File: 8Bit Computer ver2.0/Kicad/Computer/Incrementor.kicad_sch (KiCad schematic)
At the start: 5 parts, among them IC50 SN74LVC1G14DBVR, IC51 SN74LVC1G32DBVR, IC52 SN74HCS74DR, IC53 SN74HCS86DR, IC54 SN74HCS86DR

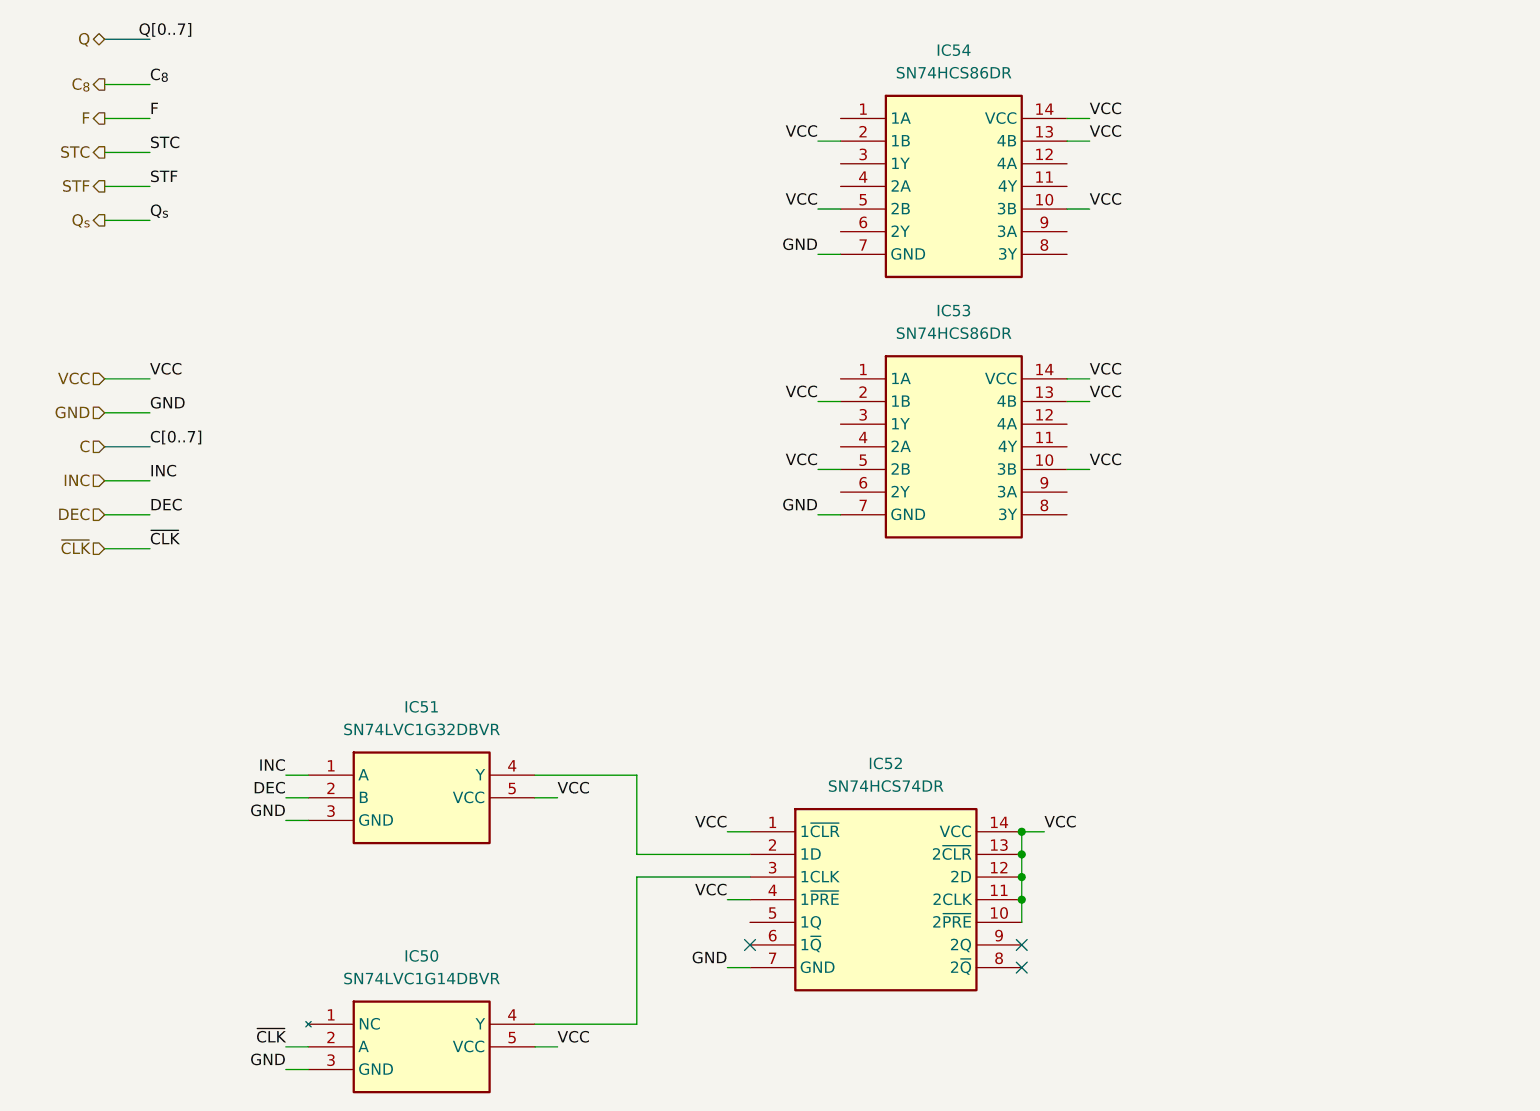
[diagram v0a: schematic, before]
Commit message: parts,Kicad
parts:
changed 8xDlatch HCS to ABT 574
waiting for SRAM CAD Model
Kicad:
imported AHC types of ICs
added ProgrammeCounter
finished Comparator
changed all HCS to AHC except 3in OR ->no AHC Version
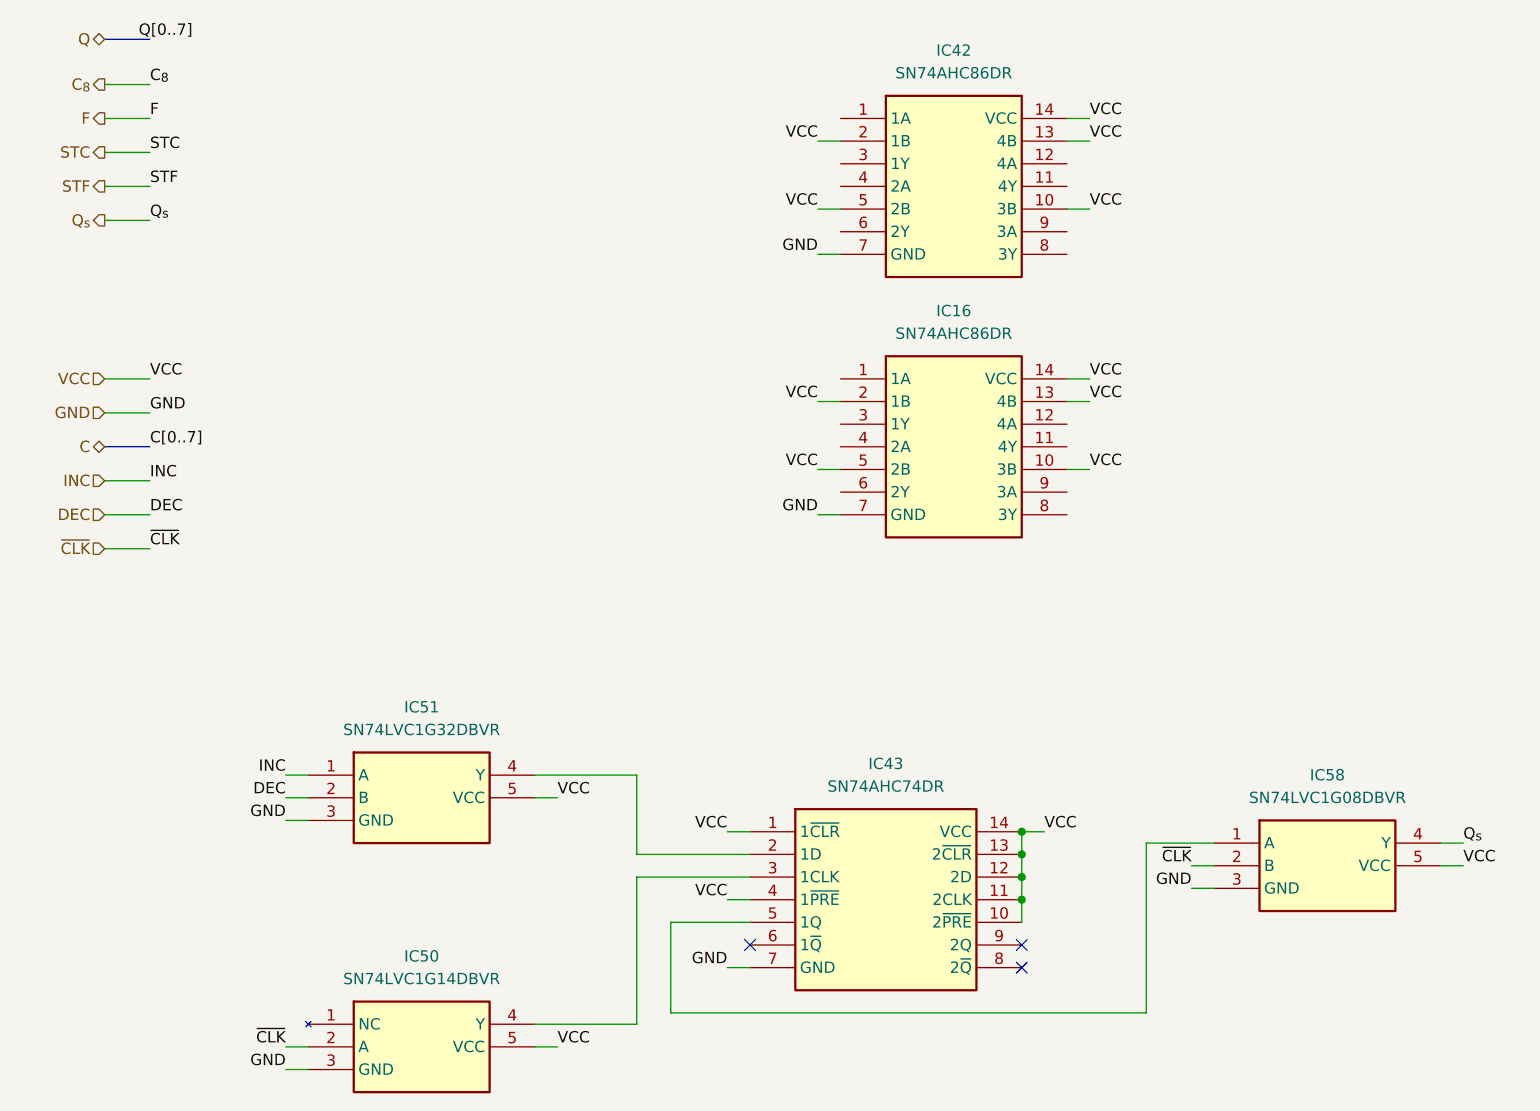
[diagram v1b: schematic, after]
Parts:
- removed IC52: SN74HCS74DR, Samacsys:SOIC127P600X175-14N, symbol Samacsys:SN74HCS74DR
- removed IC53, IC54: SN74HCS86DR, Samacsys:SOIC127P600X175-14N, symbol Samacsys:SN74HCS86DR
- added IC16, IC42: SN74AHC86DR, Samacsys:SOIC127P600X175-14N, symbol Samacsys:SN74AHC86DR
- added IC43: SN74AHC74DR, Samacsys:SOIC127P600X175-14N, symbol Samacsys:SN74AHC74DR
- added IC58: SN74LVC1G08DBVR, Samacsys:SOT95P280X145-5N, symbol Samacsys:SN74LVC1G08DBVR
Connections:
- net GND: now also IC16.7 (GND), IC42.7 (GND), IC43.7 (GND), IC58.3 (GND)
- net Q_{s}: now also IC58.4 (Y)
- net VCC: now also IC16.10 (3B), IC16.13 (4B), IC16.14 (VCC), IC16.2 (1B), IC16.5 (2B), IC42.10 (3B), IC42.13 (4B), IC42.14 (VCC), IC42.2 (1B), IC42.5 (2B), IC43.1 (1~{CLR}), IC43.10 (2~{PRE}), IC43.11 (2CLK), IC43.12 (2D), IC43.13 (2~{CLR}), IC43.14 (VCC), IC43.4 (1~{PRE}), IC58.5 (VCC)
- net ~{CLK}: now also IC58.2 (B)
- net at IC51.4 (Y): now also IC43.2 (1D)
- net at IC50.4 (Y): now also IC43.3 (1CLK)
- new net: IC43.5 (1Q), IC58.1 (A)

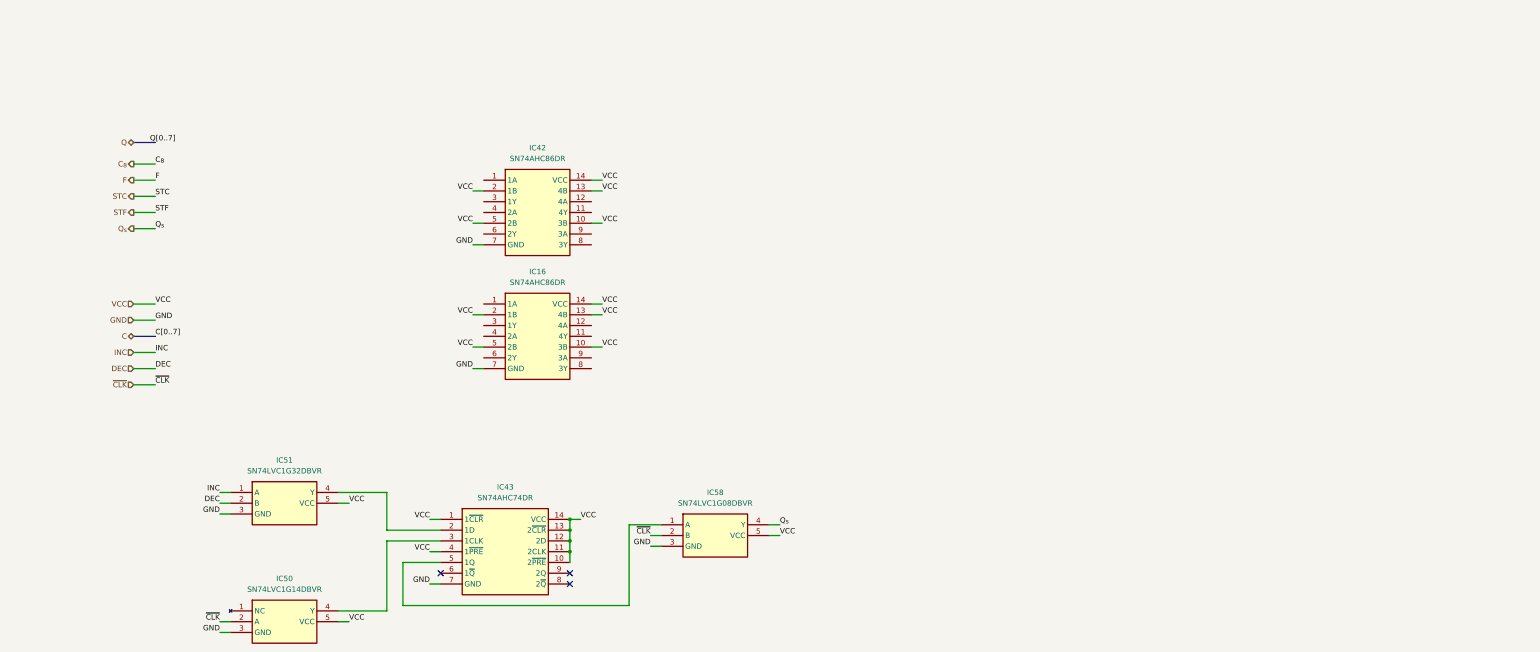
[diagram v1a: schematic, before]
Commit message: partsList, Kicad
parts:
added faster Comparator 521
added 1CH XOR
added 8Bit and 16Bit Driver 245, 16245
->they need pullUp resistors for High-Z when power on
Kicad:
included SRAM CAD Model AS7C1024
included some CAD Models
added Register 1 0x20 and 0x21
finished Incrementor
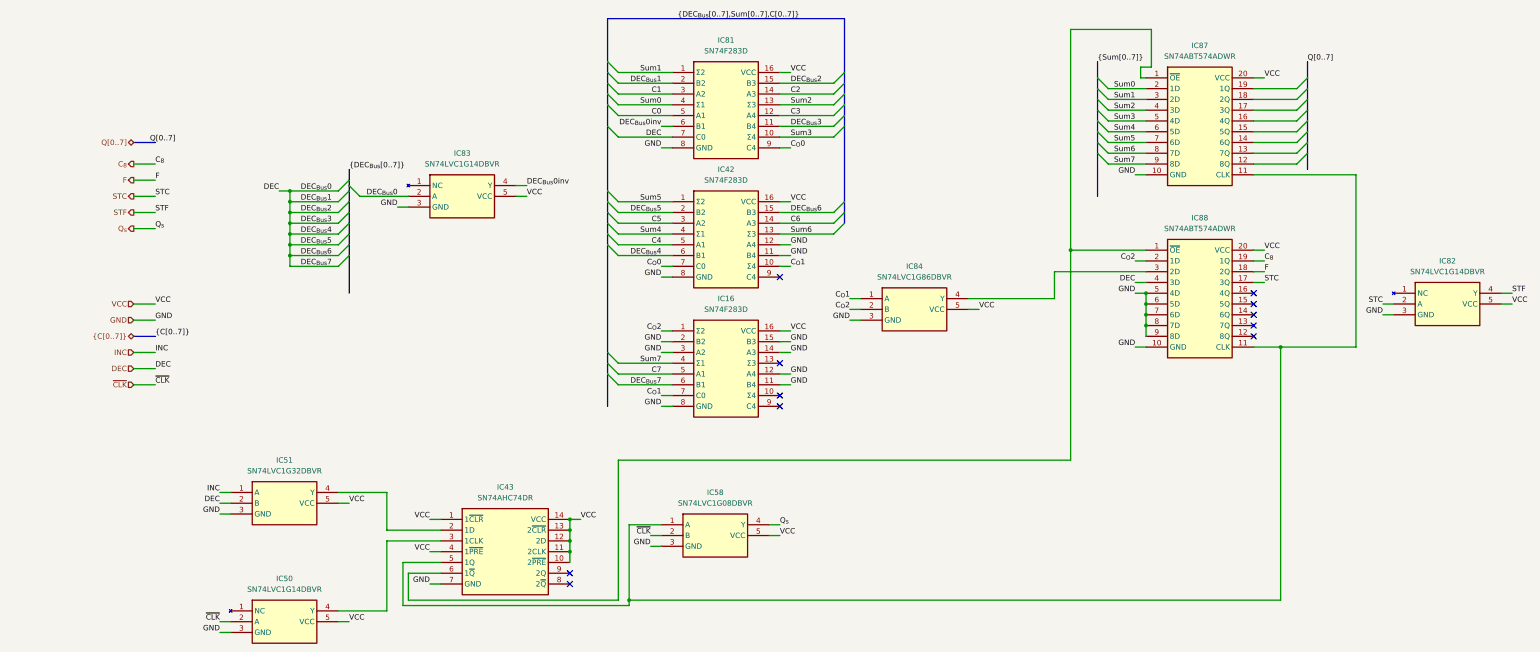
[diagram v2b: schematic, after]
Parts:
- removed IC16, IC42: SN74AHC86DR, Samacsys:SOIC127P600X175-14N, symbol Samacsys:SN74AHC86DR
- added IC16, IC42, IC81: SN74F283D, Samacsys:SOIC127P600X175-16N, symbol Samacsys:SN74F283D
- added IC82, IC83: SN74LVC1G14DBVR, Samacsys:SOT95P280X145-5N, symbol Samacsys:SN74LVC1G14DBVR
- added IC84: SN74LVC1G86DBVR, Samacsys:SOT95P280X145-5N, symbol Samacsys:SN74LVC1G86DBVR
- added IC87, IC88: SN74ABT574ADWR, Samacsys:SOIC127P1030X265-20N, symbol Samacsys:SN74ABT574ADWR
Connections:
- net C_{8}: now also IC88.19 (1Q)
- net DEC: now also IC16.6 (B1), IC42.15 (B3), IC42.2 (B2), IC42.6 (B1), IC81.11 (B4), IC81.15 (B3), IC81.2 (B2), IC81.7 (C0), IC83.2 (A), IC88.4 (3D)
- net F: now also IC88.18 (2Q)
- net GND: now also IC16.11 (B4), IC16.12 (A4), IC16.14 (A3), IC16.15 (B3), IC16.2 (B2), IC16.3 (A2), IC16.8 (GND), IC42.11 (B4), IC42.12 (A4), IC42.8 (GND), IC81.8 (GND), IC82.3 (GND), IC83.3 (GND), IC84.3 (GND), IC87.10 (GND), IC88.10 (GND), IC88.5 (4D), IC88.6 (5D), IC88.7 (6D), IC88.8 (7D), IC88.9 (8D)
- net STC: now also IC82.2 (A), IC88.17 (3Q)
- net STF: now also IC82.4 (Y)
- net VCC: now also IC16.16 (VCC), IC42.16 (VCC), IC81.16 (VCC), IC82.5 (VCC), IC83.5 (VCC), IC84.5 (VCC), IC87.20 (VCC), IC88.20 (VCC)
- net at IC43.5 (1Q), IC58.1 (A): now also IC87.11 (CLK), IC88.11 (CLK)
- net at IC43.6 (1~{Q}): now also IC87.1 (~{OE}), IC88.1 (~{OE})
- new net: IC84.4 (Y), IC88.3 (2D)
- new net C0: IC81.5 (A1)
- new net C1: IC81.3 (A2)
- new net C2: IC81.14 (A3)
- new net C3: IC81.12 (A4)
- new net C4: IC42.5 (A1)
- new net C5: IC42.3 (A2)
- new net C6: IC42.14 (A3)
- new net C7: IC16.5 (A1)
- new net C_{O}0: IC42.7 (C0), IC81.9 (C4)
- new net C_{O}1: IC16.7 (C0), IC42.10 (Σ4), IC84.1 (A)
- new net C_{O}2: IC16.1 (Σ2), IC84.2 (B), IC88.2 (1D)
- new net DEC_{Bus}0inv: IC81.6 (B1), IC83.4 (Y)
- new net Sum0: IC81.4 (Σ1), IC87.2 (1D)
- new net Sum1: IC81.1 (Σ2), IC87.3 (2D)
- new net Sum2: IC81.13 (Σ3), IC87.4 (3D)
- new net Sum3: IC81.10 (Σ4), IC87.5 (4D)
- new net Sum4: IC42.4 (Σ1), IC87.6 (5D)
- new net Sum5: IC42.1 (Σ2), IC87.7 (6D)
- new net Sum6: IC42.13 (Σ3), IC87.8 (7D)
- new net Sum7: IC16.4 (Σ1), IC87.9 (8D)
- no-connect marks 3 -> 11

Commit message: Kicad
added Register 2(0x22 u 0x23) and 3(0x13 u 0x14)
added BarrelShiftRegister
added AdderSubstractor
added cmd Comparators to the bitwise and binary Logic
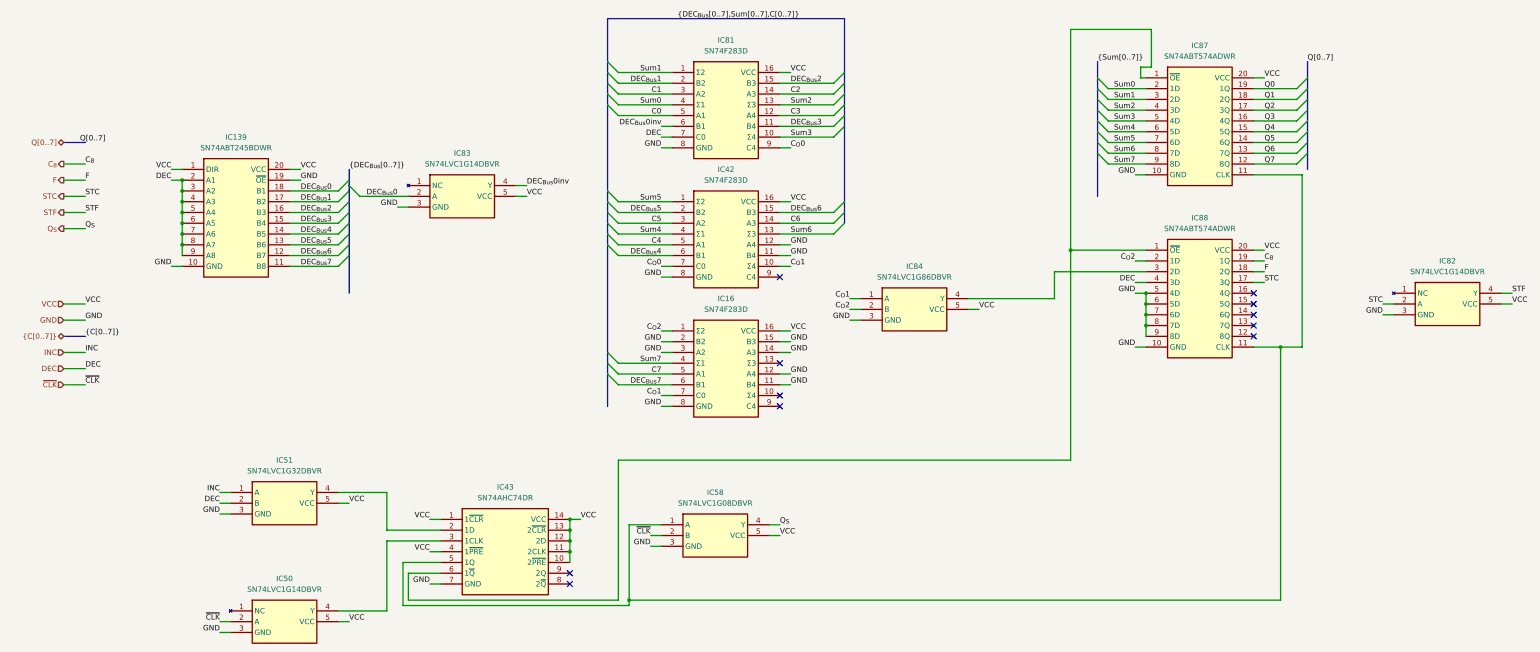
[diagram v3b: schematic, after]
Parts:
- added IC139: SN74ABT245BDWR, Samacsys:SOIC127P1030X265-20N, symbol Samacsys:SN74ABT245BDWR
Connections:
- net DEC: now also IC139.2 (A1), IC139.3 (A2), IC139.4 (A3), IC139.5 (A4), IC139.6 (A5), IC139.7 (A6), IC139.8 (A7), IC139.9 (A8); no longer IC16.6 (B1), IC42.15 (B3), IC42.2 (B2), IC42.6 (B1), IC81.11 (B4), IC81.15 (B3), IC81.2 (B2), IC83.2 (A)
- net GND: now also IC139.10 (GND), IC139.19 (~{OE})
- net VCC: now also IC139.1 (DIR), IC139.20 (VCC)
- net Q7: now reaches IC87.12 (8Q)
- net Q6: now reaches IC87.13 (7Q)
- net Q5: now reaches IC87.14 (6Q)
- net Q4: now reaches IC87.15 (5Q)
- net Q3: now reaches IC87.16 (4Q)
- net Q2: now reaches IC87.17 (3Q)
- net Q1: now reaches IC87.18 (2Q)
- net Q0: now reaches IC87.19 (1Q)
- net Q_{s} renamed Q_{S}
- new net DEC_{Bus}0: IC139.18 (B1), IC83.2 (A)
- new net DEC_{Bus}1: IC139.17 (B2), IC81.2 (B2)
- new net DEC_{Bus}2: IC139.16 (B3), IC81.15 (B3)
- new net DEC_{Bus}3: IC139.15 (B4), IC81.11 (B4)
- new net DEC_{Bus}4: IC139.14 (B5), IC42.6 (B1)
- new net DEC_{Bus}5: IC139.13 (B6), IC42.2 (B2)
- new net DEC_{Bus}6: IC139.12 (B7), IC42.15 (B3)
- new net DEC_{Bus}7: IC139.11 (B8), IC16.6 (B1)
